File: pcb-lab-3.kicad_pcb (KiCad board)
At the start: 2 copper layers, 93 parts, among them J1 USB_B_Micro, J2 Conn_01x02, J3 Conn_01x02, J301 USB_B_Micro, J302 USB_B_Micro, J303 Conn_01x02, J304 Conn_01x02, J305 Conn_01x02, J306 Conn_01x02, J307 Conn_01x02, J308 Conn_01x02, J309 Conn_01x03_Female, J310 Conn_01x02_Female, J311 Conn_01x03_Female, J4 Conn_01x02, J401 USB_B_Micro, J402 Conn_01x02, J403 Conn_01x02, J404 Conn_01x02, J405 Conn_01x03, J406 Conn_01x02_Female, J407 Conn_01x02, J5 Conn_01x03, J501 Conn_01x02, J502 Conn_01x02, J503 Conn_01x02, J6 Conn_01x04, Q1 Q_NMOS_GSD, Q301 Q_NMOS_GSD, Q302 Q_NMOS_GSD, Q401 Q_NMOS_GSD, U1 NCS2333, U2 MCP4011, U301 NCS2333, U302 INA181, U401 NCS2333, U402 INA181, U501 BCR421U

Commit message: Complete routing (-GND) of 3rd an 4th circuits
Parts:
- moved J406 0.56 mm to (136.2, 113.0)
- moved R403 0.56 mm to (134.0, 114.2)
- moved R408 0.56 mm to (131.5, 114.2)
- moved C401 0.35 mm to (142.8, 104.2)
- moved JP402 0.35 mm to (147.8, 106.2)
- moved U401 0.35 mm to (139.8, 108.2)
- moved R404 0.25 mm to (147.5, 104.2)
- moved C406 0.24 mm to (145.2, 108.2)
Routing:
- net +5V: track 121.6 -> 176.2 mm, vias 6 -> 8
- net GND: track 42.6 -> 83.4 mm
- net uC_ADC: track 0.00 -> 30.0 mm, vias 0 -> 1
- net Net-(J406-Pad2): track 0.00 -> 14.6 mm
- net Net-(JP403-Pad2): track 0.00 -> 12.0 mm
- net Net-(C404-Pad1): track 5.77 -> 17.2 mm, vias 0 -> 2
- net Net-(JP402-Pad2): track 0.00 -> 10.7 mm
- net Net-(RV501-Pad1): track 0.00 -> 9.92 mm
- net Net-(C406-Pad1): track 0.00 -> 8.85 mm
- net LOAD5+: track 0.00 -> 7.95 mm
- net Net-(C406-Pad2): track 0.00 -> 7.25 mm
- net LOAD5-: track 0.00 -> 6.42 mm
- net Net-(J406-Pad1): track 4.43 -> 10.6 mm
- net uC_LED_EN: track 0.00 -> 4.22 mm
- net LOAD4-: track 0.00 -> 3.57 mm

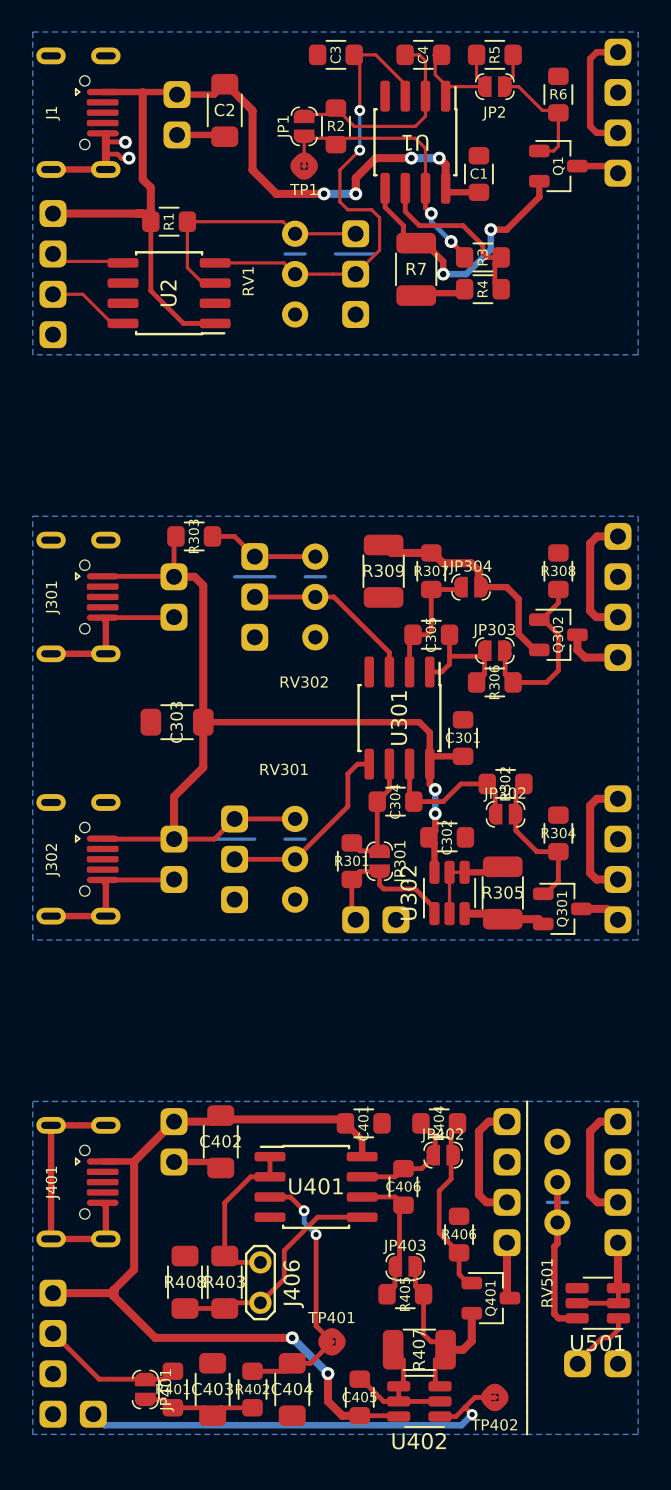
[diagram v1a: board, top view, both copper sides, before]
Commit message: Ground vias
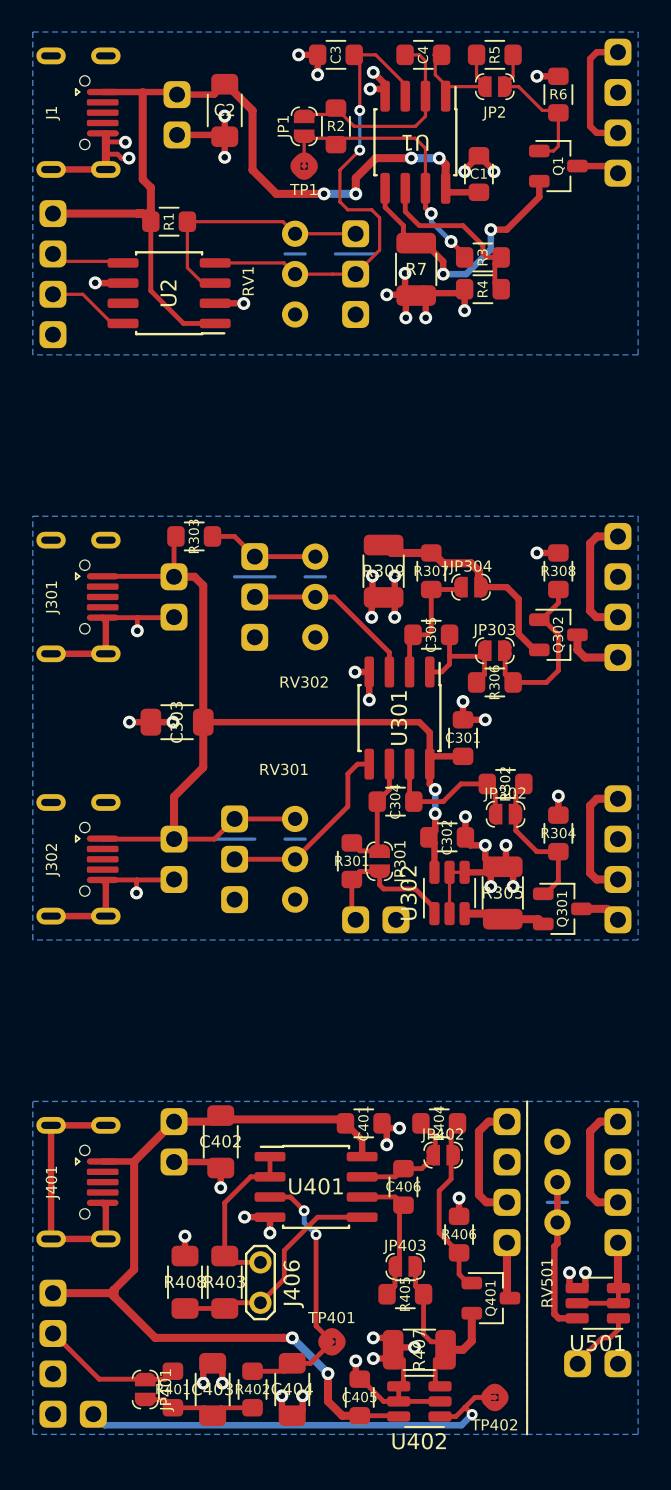
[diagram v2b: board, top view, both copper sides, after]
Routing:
- net GND: track 83.4 -> 148.3 mm, vias 2 -> 54

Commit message: Minor tuning
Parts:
- moved J401 20.3 mm to (121.9, 87.6)
- moved J402 20.3 mm to (130.8, 83.8)
- moved J403 20.3 mm to (151.8, 83.8)
- moved J405 20.3 mm to (123.2, 99.7)
- moved J407 20.3 mm to (125.7, 102.2)
- moved J502 20.3 mm to (158.8, 83.8)
- moved RV501 20.3 mm to (154.9, 87.6)
- moved C401 20.3 mm to (142.8, 83.9)
- moved C402 20.3 mm to (133.8, 85.1)
- moved C403 20.3 mm to (133.2, 100.7)
- moved C404 20.3 mm to (138.2, 100.7)
- moved C405 20.3 mm to (142.5, 101.2)
- moved C406 20.3 mm to (145.2, 87.9)
- moved J404 20.3 mm to (151.8, 88.9)
- moved J406 20.3 mm to (136.2, 92.7)
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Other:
- board outline added: 38.1 x 67.9 mm

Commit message: Top and bottom silkscreen
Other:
- board text added: "0.1"
- board text added: "0.1u"
- board text added: "100"
- board text added: "100R"
- board text added: "100k"
- board text added: "10k"
- board text added: "1R"
- board text added: "1k"
- board text added: "1u"
- board text added: "3.3k"
- board text added: "50k"
- board text added: "5V"
- board text added: "BCR421U"
- board text added: "BCR421U current source"
- board text added: "Current source with INA181 pre-amp max: 50 mA"
- board text added: "EN"
- board text added: "G"
- board text added: "GND"
- board text added: "INA181A3 for uC ADC"
- board text added: "L+"
- board text added: "L-"
- board text added: "MCP4011"
- board text added: "MCP4011 controlled current source max: 53 mA"
- board text added: "NCS2333"
- board text added: "NMOS"
- board text added: "PCB Lab #3 (C) Vlad Belous CC BY-SA 4.0"
- board text added: "Simple current source, max: 455 mA"
- board text added: "UD"
- board text added: "uC PWM controlled current source max: 49.5 mA"
- board text added: "uC_ADC"
- board text added: "uC_PWM"
- board text added: "~CS"
